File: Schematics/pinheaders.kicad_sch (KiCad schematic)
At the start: 16 parts, among them J1001 Conn_01x08_Pin, J1002 Conn_01x08_Pin, J1004 Conn_01x08_Pin, J1005 Conn_01x08_Pin, J1008 Conn_01x08_Pin, J1010 Conn_01x08_Pin, J1011 Conn_01x08_Pin, J1012 Conn_01x08_Pin, J1013 Conn_01x08_Pin, J1014 Conn_01x08_Pin, J1015 Conn_01x08_Pin, J1016 Conn_01x08_Pin, J1017 Conn_01x08_Pin, J1018 Conn_01x08_Pin, J1019 Conn_01x08_Pin, J1020 Conn_01x08_Pin

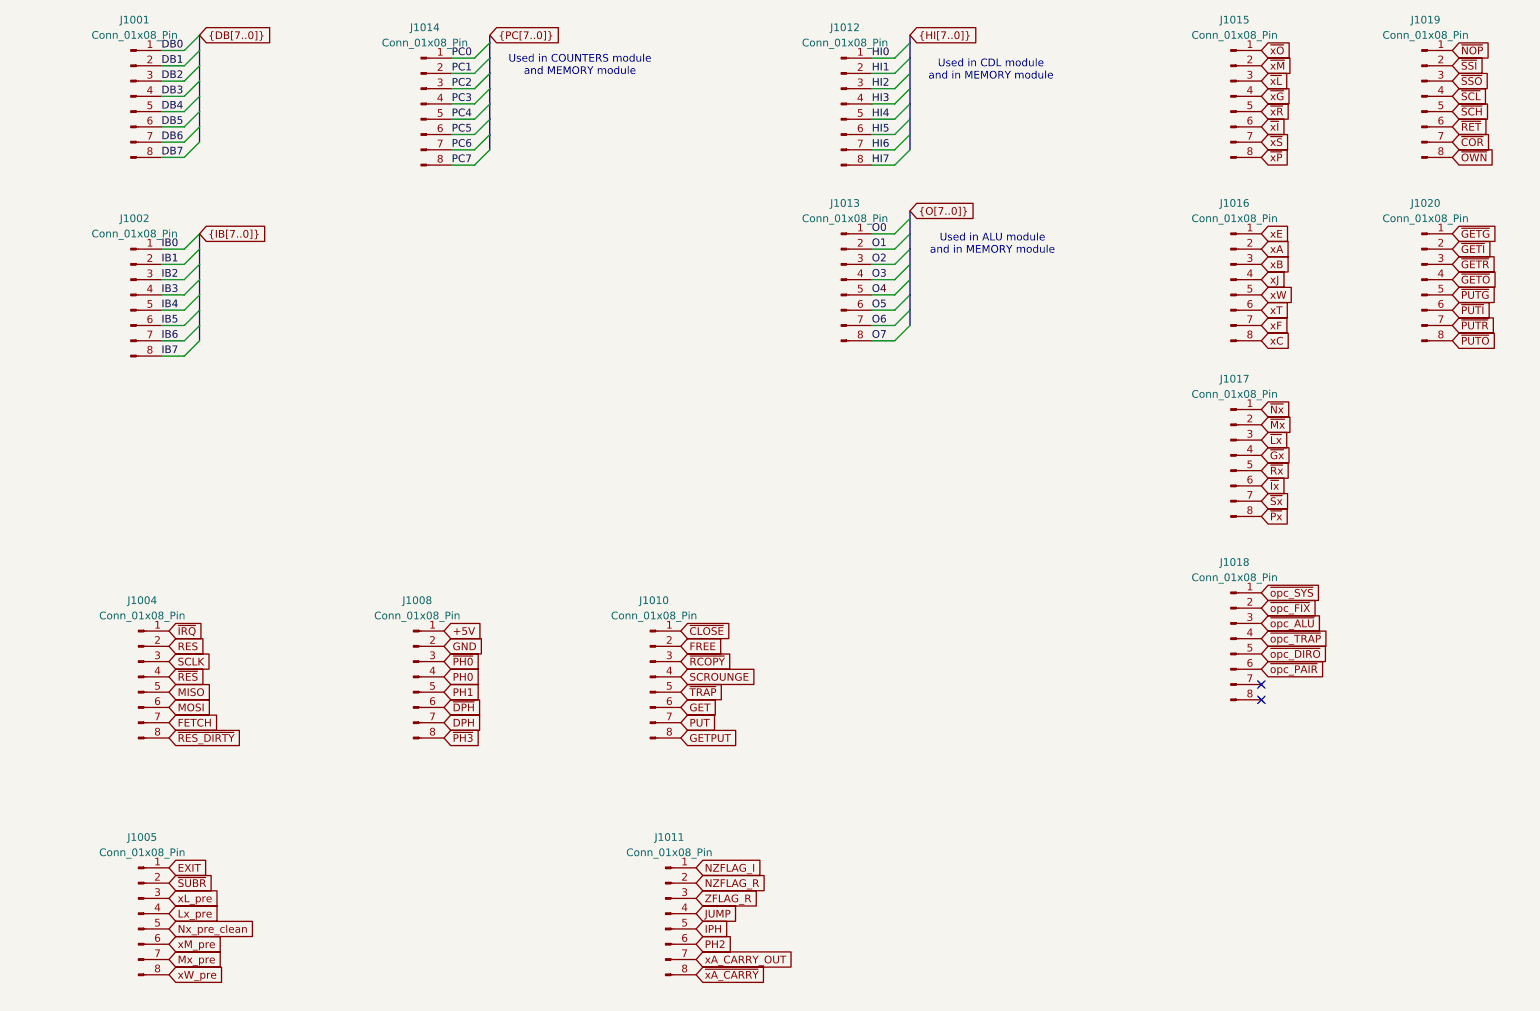
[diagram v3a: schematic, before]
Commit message: Change semantics of xB
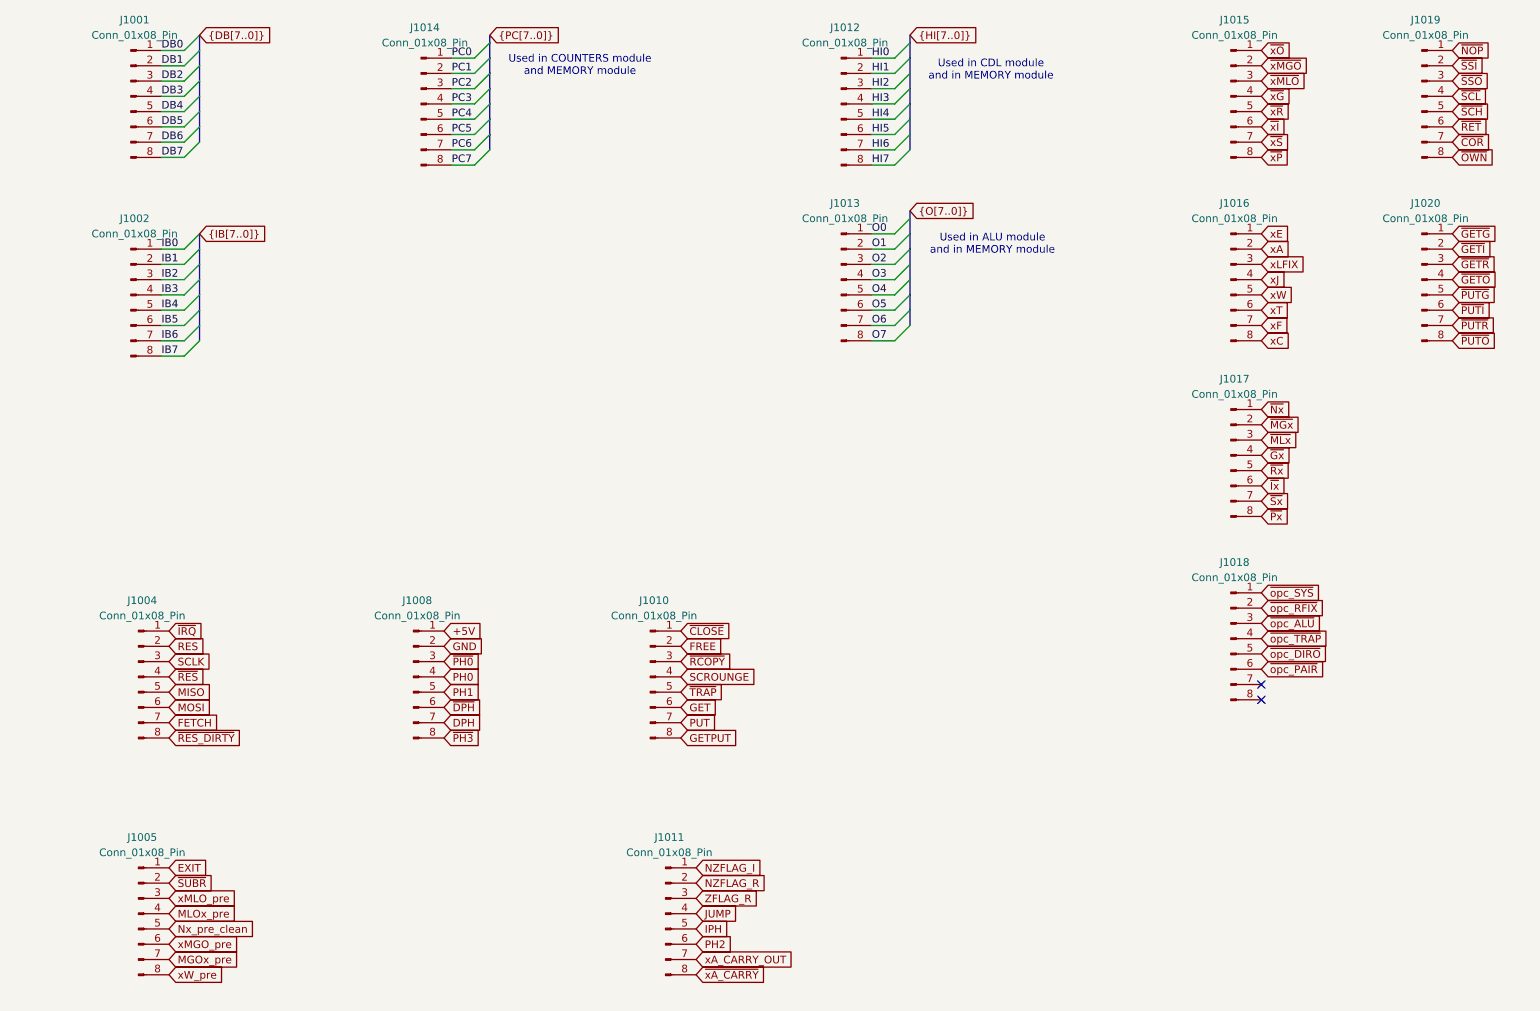
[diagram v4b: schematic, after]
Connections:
- net Lx_pre renamed MLOx_pre
- net Mx_pre renamed MGOx_pre
- net xB renamed xLFIX
- net xL_pre renamed xMLO_pre
- net xM_pre renamed xMGO_pre
- net ~{Lx} renamed ~{MLx}
- net ~{Mx} renamed ~{MGx}
- net ~{opc_FIX} renamed ~{opc_RFIX}
- net ~{xL} renamed ~{xMLO}
- net ~{xM} renamed ~{xMGO}
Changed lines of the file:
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@@
 		)
 	)
-	(global_label "~{Lx}"
+	(global_label "~{MLx}"
 		(shape input)
 		(at 226.06 88.9 0)
@@
 		)
 		(property "Intersheetrefs" "${INTERSHEET_REFS}"
-			(at 231.1014 88.9 0)
+			(at 232.5528 88.9 0)
 			(effects
 				(font
@@
 		)
 	)
-	(global_label "xL_pre"
+	(global_label "xMLO_pre"
 		(shape input)
 		(at 44.45 165.1 0)
@@
 		)
 	)
-	(global_label "xB"
+	(global_label "xLFIX"
 		(shape input)
 		(at 226.06 59.69 0)
@@
 		)
 	)
-	(global_label "Lx_pre"
+	(global_label "MLOx_pre"
 		(shape input)
 		(at 44.45 167.64 0)
@@
 		)
 	)
-	(global_label "~{xM}"
+	(global_label "~{xMGO}"
 		(shape input)
 		(at 226.06 26.67 0)
@@
 		)
 	)
-	(global_label "~{Mx}"
+	(global_label "~{MGx}"
 		(shape input)
 		(at 226.06 86.36 0)
@@
 		)
 		(property "Intersheetrefs" "${INTERSHEET_REFS}"
-			(at 231.5247 86.36 0)
+			(at 232.7947 86.36 0)
 			(effects
 				(font
@@
 		)
 	)
-	(global_label "~{opc_FIX}"
+	(global_label "~{opc_RFIX}"
 		(shape input)
 		(at 226.06 116.84 0)
@@
 		)
 	)
-	(global_label "xM_pre"
+	(global_label "xMGO_pre"
 		(shape input)
 		(at 44.45 172.72 0)
@@
 		)
 	)
-	(global_label "Mx_pre"
+	(global_label "MGOx_pre"
 		(shape input)
 		(at 44.45 175.26 0)
@@
 		)
 	)
-	(global_label "~{xL}"
+	(global_label "~{xMLO}"
 		(shape input)
 		(at 226.06 29.21 0)

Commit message: Change signal names
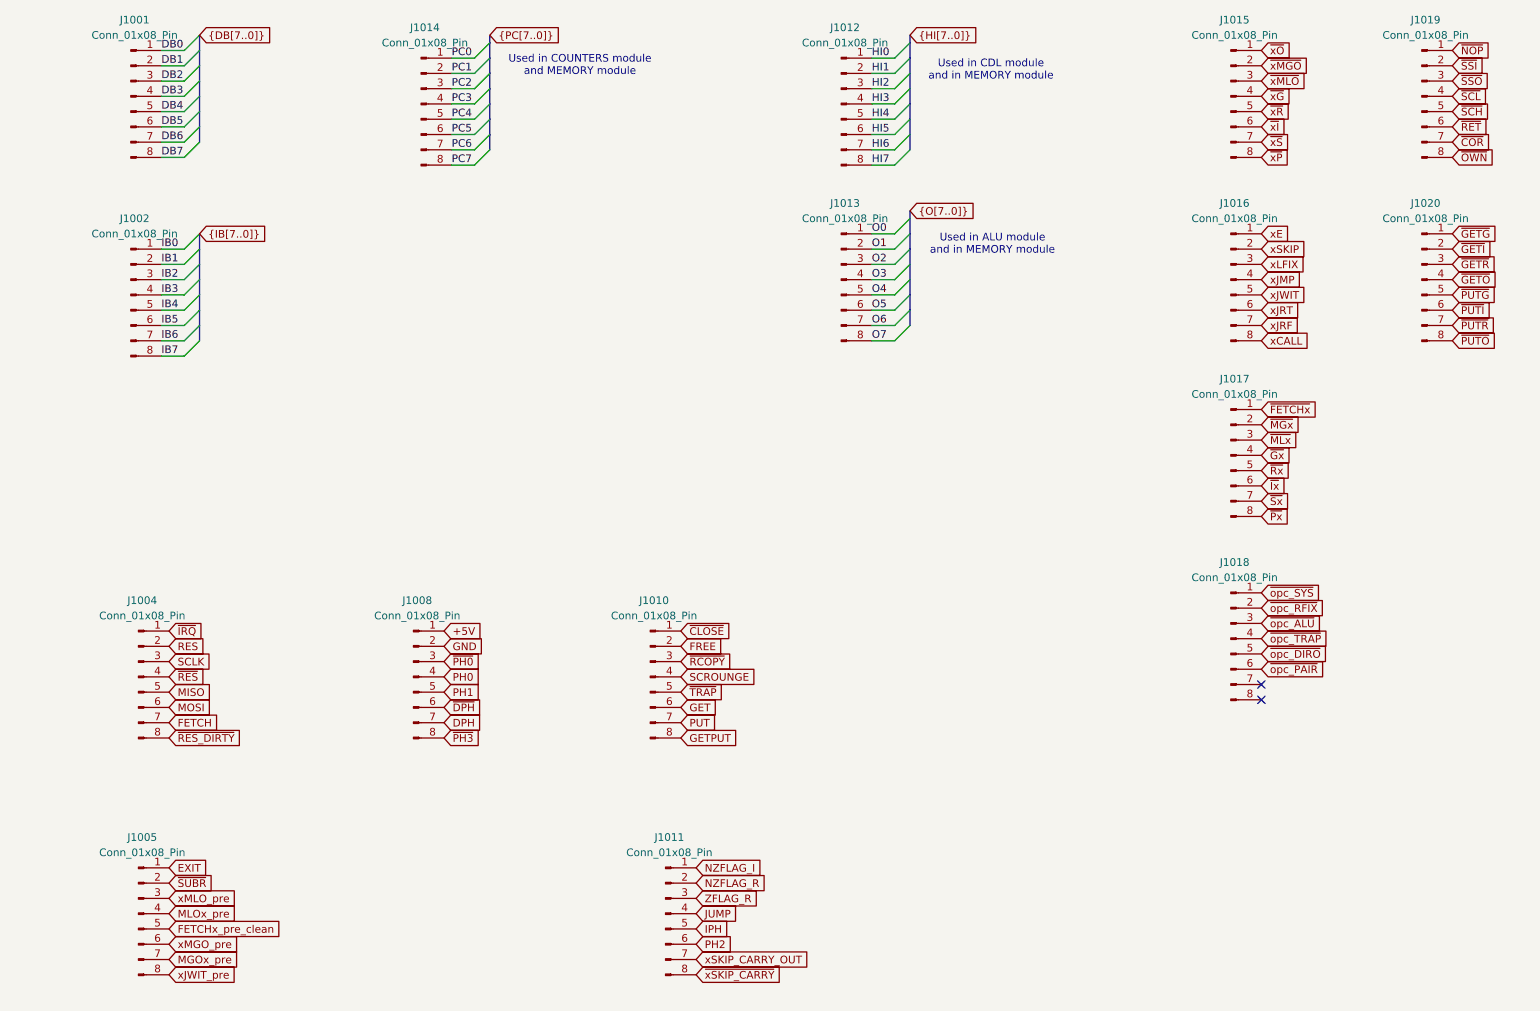
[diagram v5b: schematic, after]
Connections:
- net Nx_pre_clean renamed FETCHx_pre_clean
- net xA renamed xSKIP
- net xA_CARRY_OUT renamed xSKIP_CARRY_OUT
- net xC renamed xCALL
- net xF renamed xJRF
- net xJ renamed xJMP
- net xT renamed xJRT
- net xW renamed xJWIT
- net xW_pre renamed xJWIT_pre
- net ~{Nx} renamed ~{FETCHx}
- net ~{xA_CARRY} renamed ~{xSKIP_CARRY}
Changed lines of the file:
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@@
 		)
 	)
-	(global_label "~{xA_CARRY}"
+	(global_label "~{xSKIP_CARRY}"
 		(shape input)
 		(at 132.08 177.8 0)
@@
 		)
 	)
-	(global_label "xW_pre"
+	(global_label "xJWIT_pre"
 		(shape input)
 		(at 44.45 177.8 0)
@@
 		)
 	)
-	(global_label "xW"
+	(global_label "xJWIT"
 		(shape input)
 		(at 226.06 64.77 0)
@@
 		)
 	)
-	(global_label "xC"
+	(global_label "xCALL"
 		(shape input)
 		(at 226.06 72.39 0)
@@
 		)
 	)
-	(global_label "xT"
+	(global_label "xJRT"
 		(shape input)
 		(at 226.06 67.31 0)
@@
 		)
 	)
-	(global_label "~{Nx}"
+	(global_label "~{FETCHx}"
 		(shape input)
 		(at 226.06 83.82 0)
@@
 		)
 	)
-	(global_label "xF"
+	(global_label "xJRF"
 		(shape input)
 		(at 226.06 69.85 0)
@@
 		)
 	)
-	(global_label "xA"
+	(global_label "xSKIP"
 		(shape input)
 		(at 226.06 57.15 0)
@@
 		)
 	)
-	(global_label "Nx_pre_clean"
+	(global_label "FETCHx_pre_clean"
 		(shape input)
 		(at 44.45 170.18 0)
@@
 		)
 	)
-	(global_label "xA_CARRY_OUT"
+	(global_label "xSKIP_CARRY_OUT"
 		(shape input)
 		(at 132.08 175.26 0)
@@
 		)
 	)
-	(global_label "xJ"
+	(global_label "xJMP"
 		(shape input)
 		(at 226.06 62.23 0)

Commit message: Let defines/labels diverge from assembler mnemonics
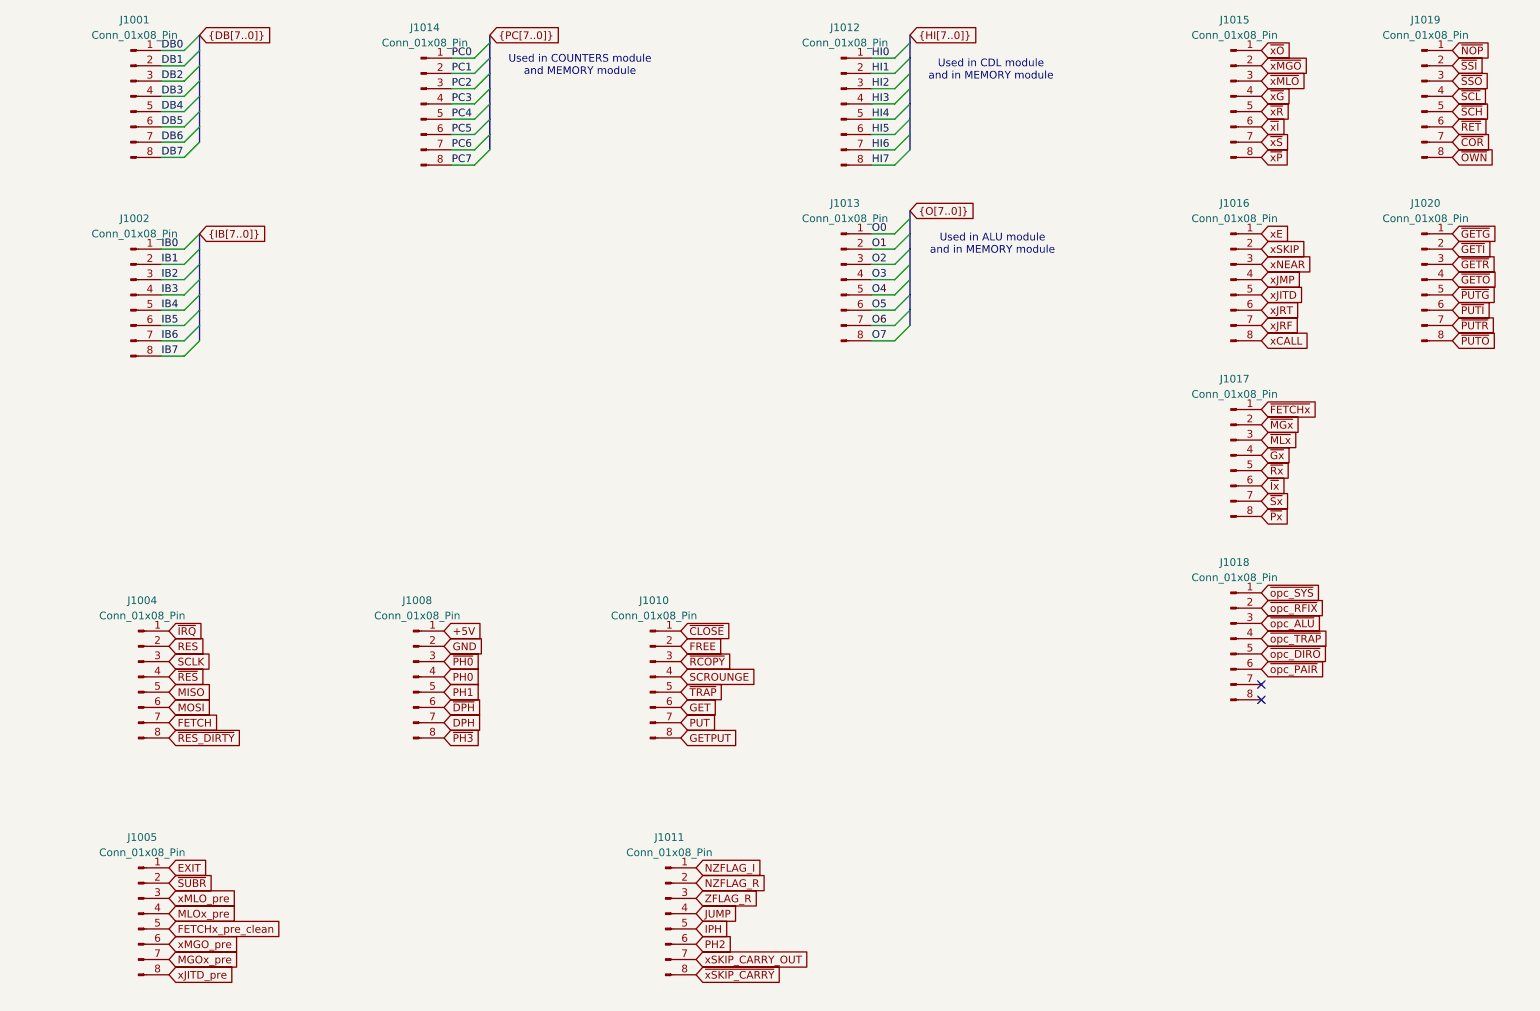
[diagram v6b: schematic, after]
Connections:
- net xJWIT renamed xJITD
- net xJWIT_pre renamed xJITD_pre
- net xLFIX renamed xNEAR
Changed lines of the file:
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@@
 		)
 	)
-	(global_label "xJWIT_pre"
+	(global_label "xJITD_pre"
 		(shape input)
 		(at 44.45 177.8 0)
@@
 		)
 	)
-	(global_label "xJWIT"
+	(global_label "xJITD"
 		(shape input)
 		(at 226.06 64.77 0)
@@
 		)
 	)
-	(global_label "xLFIX"
+	(global_label "xNEAR"
 		(shape input)
 		(at 226.06 59.69 0)
